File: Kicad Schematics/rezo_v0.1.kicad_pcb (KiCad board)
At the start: 2 copper layers, 15 parts, among them J1 Battery, J2 LRA_R, J3 LRA_L, SW2 SW_Push, U1 XIAO-nRF52840-SMD, U2 DRV2605LDGSR, U3 DRV2605LDGSR

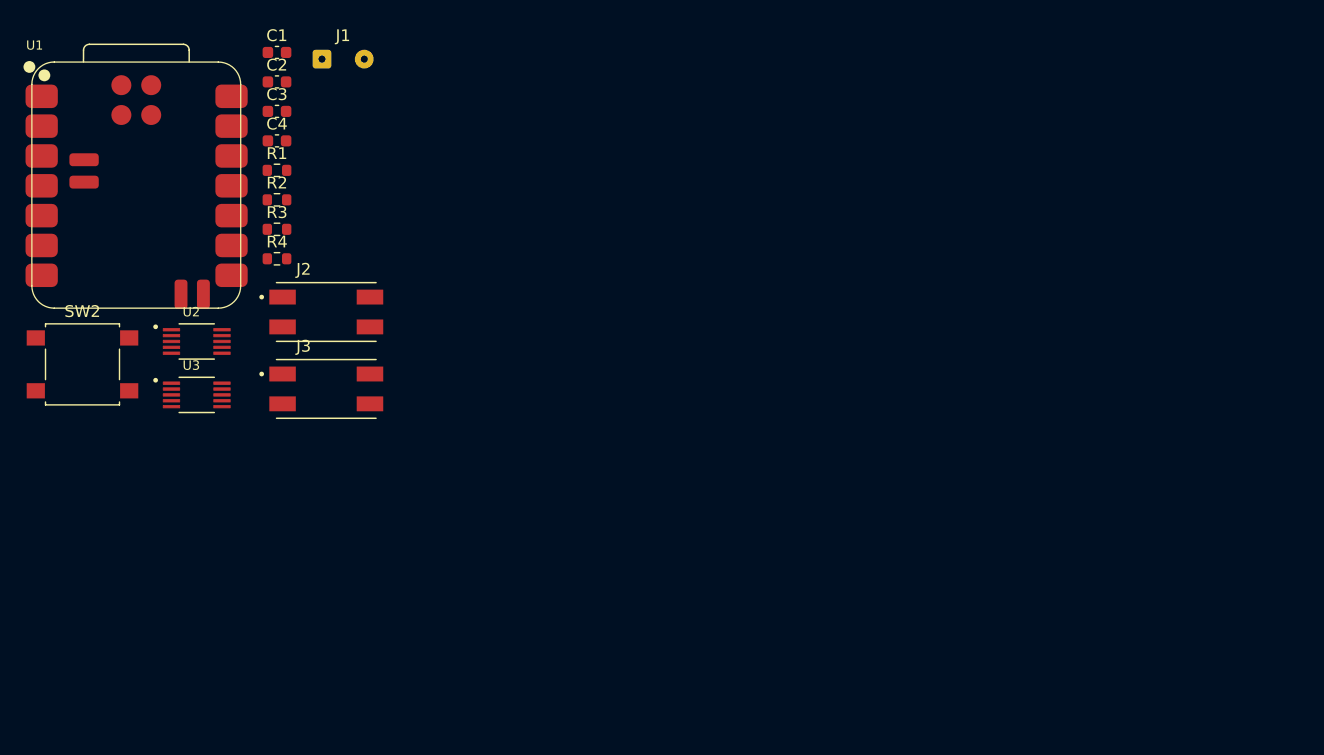
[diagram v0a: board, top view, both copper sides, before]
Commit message: Tune KiCad DRC constraints and mask settings; generate DRC/ERC reports
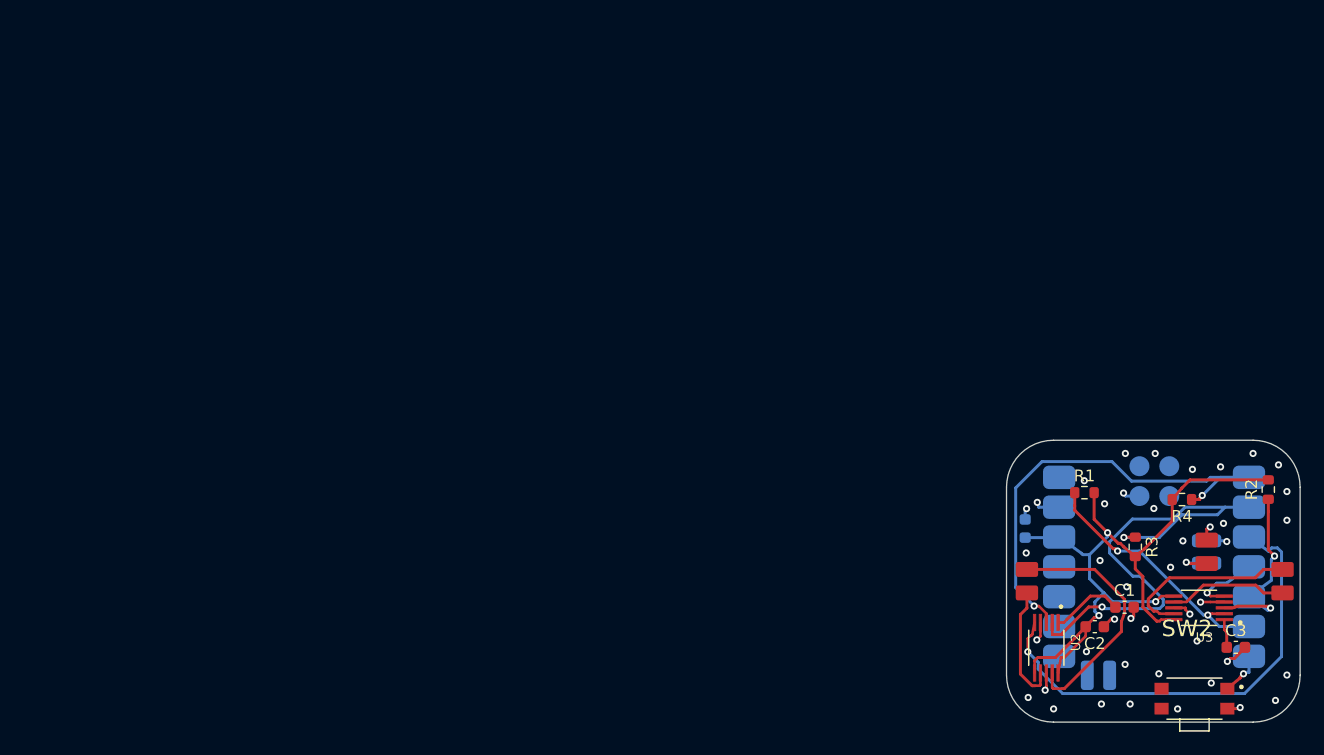
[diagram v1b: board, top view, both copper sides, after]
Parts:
- C4, U1: moved to B.Cu
- J1: footprint Connector_Wire:SolderWire-0.1sqmm_1x02_P3.6mm_D0.4mm_OD1mm -> Connector:01x02_Pad_2.0mm
- J2, J3: footprint Connector:BOURNS_70AAJ-2-M0 -> Connector:01x02_Pad_2.0mm
- SW2: footprint Button_Switch_SMD:SW_SPST_B3S-1000 -> Button_Switch_SMD:SW_TL1014AF160QG
- moved SW2 98.9 mm to (116.0, 72.0)
- moved C3 93.5 mm to (119.5, 67.6)
- moved U1 92.5 mm to (112.5, 60.8), turned to 180 degrees
- moved R2 87.9 mm to (122.3, 54.2), turned to 90 degrees
- moved U3 87.2 mm to (116.4, 64.3), turned to 180 degrees
- moved C1 86.3 mm to (110.1, 64.2)
- moved J1 86.0 mm to (116.8, 59.5), turned to -90 degrees
- moved C2 83.7 mm to (107.5, 65.9), turned to 180 degrees
- moved J3 83.3 mm to (123.8, 62.0), turned to 90 degrees
- moved R4 79.7 mm to (114.9, 55.0), turned to 180 degrees
- moved R3 77.9 mm to (111.0, 59.1), turned to 270 degrees
- moved U2 76.9 mm to (103.4, 67.7), turned to 270 degrees
- moved R1 74.0 mm to (106.6, 54.5)
- moved C4 71.7 mm to (101.6, 57.5), turned to 270 degrees
- moved J2 64.2 mm to (102.0, 62.0), turned to 90 degrees
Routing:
- net /3V3: track 0.00 -> 64.2 mm, vias 0 -> 3
- net /SCL_R: track 0.00 -> 43.1 mm, vias 0 -> 2
- net /SDA_R: track 0.00 -> 40.1 mm, vias 0 -> 2
- net /EN_R: track 0.00 -> 39.7 mm, vias 0 -> 1
- net /SCL_L: track 0.00 -> 21.9 mm, vias 0 -> 2
- net Net-(J2-Pin_2): track 0.00 -> 21.3 mm
- net GND: track 0.00 -> 20.0 mm, vias 0 -> 43
- net /SDA_L: track 0.00 -> 15.9 mm, vias 0 -> 2
- net Net-(J3-Pin_2): track 0.00 -> 15.5 mm
- net Net-(J2-Pin_1): track 0.00 -> 10.3 mm
- net Net-(J3-Pin_1): track 0.00 -> 10.1 mm
- net Net-(U2-REG): track 0.00 -> 6.23 mm
- net /EN_L: track 0.00 -> 5.94 mm, vias 0 -> 1
- net Net-(U1-P1.11_D6_TX): track 0.00 -> 3.78 mm, vias 0 -> 1
- net Net-(J1-Pin_2): track 0.00 -> 3.55 mm, vias 0 -> 1
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- added copper zone on In1.Cu, net GND
- added copper zone on In2.Cu, net GND
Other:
- board outline added: 25 x 24 mm
- copper layers 2 -> 4
- rule solder_mask_min_width: 0.1 -> 0
